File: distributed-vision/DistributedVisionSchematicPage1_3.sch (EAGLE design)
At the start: 114 parts, among them J1 RASPBERRRY_COMPUTE_CM3, J2 RASPBERRRY_COMPUTE_CM3, J3 XS10, J4 10029449-111RLF, J5 10029449-111RLF, Q1 AP2331SA-7, Q2 BSS127, Q3 BSS127, Q4 BJT-NPN_, U1 TPS70625DBVR, U2 LM26420XMH, U3 TPD13S523, U4 ESD224, X1 JST-XH-02-PIN-LONG-PAD

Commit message: Update DistributedVisionSchematicPage1_3.sch
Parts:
- removed U3: TPD13S523, distributed-vision:TPD13S523
- added C14: (no value), rcl:C-USC0603
- added J6: DM3D-SF, distributed-vision:DM3D-SF
- added J7: 10029449-111RLF, distributed-vision:10029449-111RLF
- added Q5: PSMN014-40YS, RoboJackets-Discrete:PSMN014-40YS
- added R56: 47k, RoboJackets-Resistors:ERJ-L06KF50MV
- added RN1, RN2: (no value), RoboJackets-Resistors:RA-82506
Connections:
- new net N$42: J2A.HDMI_CLK_P, J7.10
- new net N$43: J2A.HDMI_CLK_N, J7.12
- new net N$44: J2A.HDMI_SDA, J7.16
- new net N$45: J7.19, Q5.G, R56.PIN2
- net +5V: now also C14.1, J7.18
- net GND: now also C14.2, J7.11, J7.17, J7.2, J7.5, J7.8, Q5.D, R56.PIN1, U4.GND@1, U4.GND@2
- net N$24: now also J7.1; no longer U3.D2+
- net N$25: now also J7.3; no longer U3.D2-
- net N$26: now also J2A.HDMI_D1_P, J7.4; no longer J2A.HDMI_D1_N, U3.D1-
- net N$27: now also J2A.HDMI_D1_N, J7.6; no longer J2A.HDMI_D1_P, U3.D1+
- net N$28: now also J7.7; no longer U3.D0+
- net N$29: now also J7.9; no longer U3.D0-
- net N$30: now also Q5.S
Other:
- note added: "5V FROM USB BOOT"
- note added: "CM1 VBAT = 3v3"
- note added: "CM3 VBAT = 5v"
- note added: "CONNECTOR FOR CAMERA"
- note added: "DAC VCC"
- note added: "DUAL BUCK 1V8 AND 3V3"
- note added: "GPIO BANK0/1 VCC"
- note added: "HDMI POWER"
- note added: "PLACE NEAR COMPUTE MODEL"
- note added: "RASPBERRY PI HEADER"
- note added: "SELECT VBAT for CM1 or CM3"
- note added: "USB BOOT ENABLE"
- moved on the sheet: C10, C102, C103, C12, C13, C15, C17, C18, C19, C21, C22, C23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

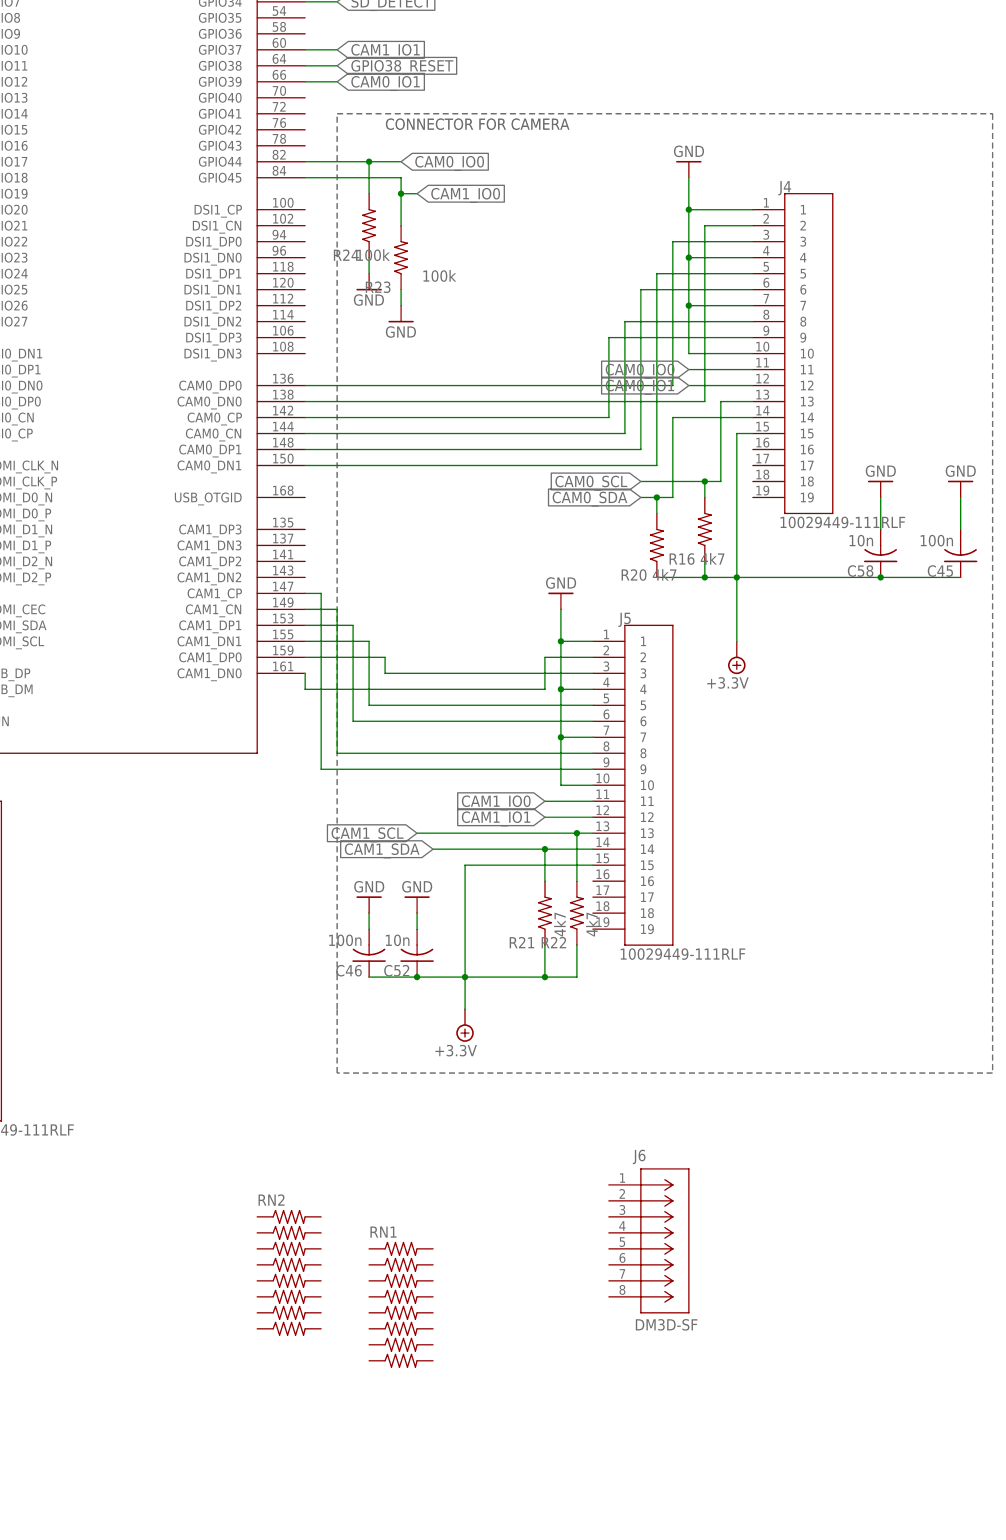
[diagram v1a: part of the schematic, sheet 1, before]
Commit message: Disb Vision Library Edit/Schematic Update
Edited Pins 4,6,10,12,14,16,18,22,24 to SDX_ for MicroSD
Finish Micro_SD part of Schematic on Pg 1
Replaced BJT with JP1 on Pg 3
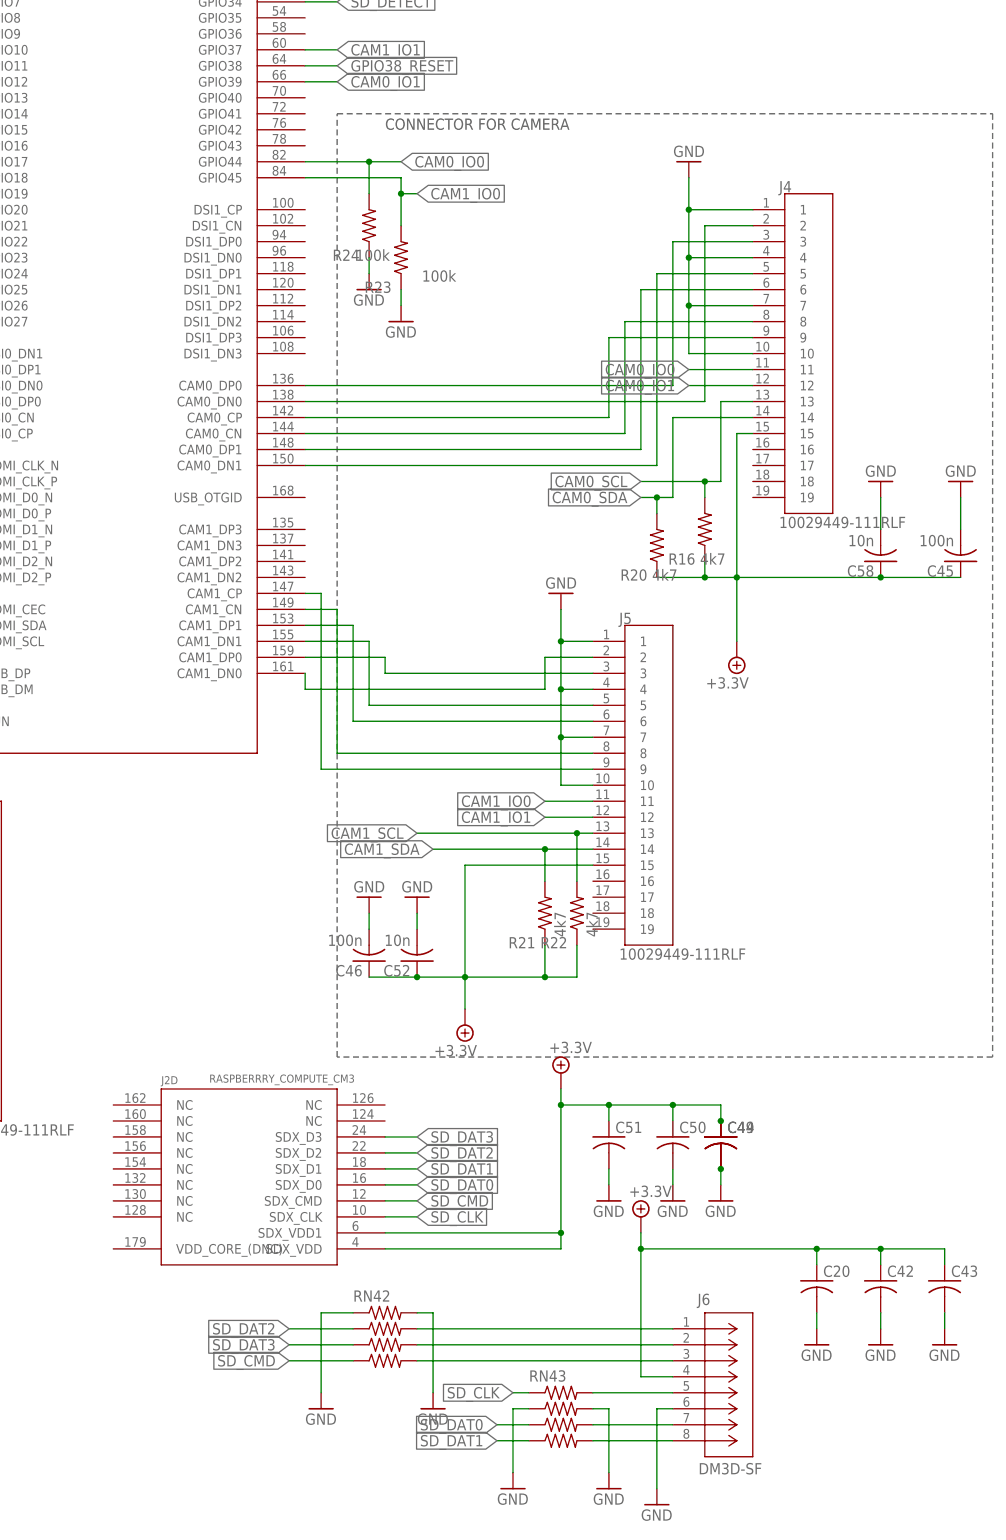
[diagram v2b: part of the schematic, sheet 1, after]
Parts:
- removed L3: (no value), RoboJackets-Inductors:INDUCTOR_0805
- removed Q4: BJT-NPN_, RoboJackets-Discrete:BJT-NPN_
- removed RN1, RN2: (no value), RoboJackets-Resistors:RA-82506
- added C20, C42, C43, C44, C49, C50, C51: (no value), rcl:C-USC0603
- added JP1: (no value), RoboJackets-Connectors:PINHD-1X2
- added L8: 1.3A 120r, RoboJackets-Inductors:INDUCTOR_0805
- added RN42, RN43: (no value), RoboJackets-Resistors:RA-41206
- L1: value 1.3A -> 1uH
- L2: value (none) -> 1uH
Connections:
- new net N$46: J6.1, RN42.4
- new net N$47: J6.2, RN42.6
- new net N$48: J6.3, RN42.8
- new net N$49: J6.5, RN43.2
- new net N$50: J6.7, RN43.6
- new net N$51: J6.8, RN43.8
- new net SD_CLK: J2D.SDX_CLK, RN43.1
- new net SD_CMD: J2D.SDX_CMD, RN42.7
- new net SD_DAT0: J2D.SDX_D0, RN43.5
- new net SD_DAT1: J2D.SDX_D1, RN43.7
- new net SD_DAT2: J2D.SDX_D2, RN42.3
- new net SD_DAT3: J2D.SDX_D3, RN42.5
- net +3.3V: now also C20.1, C42.1, C43.1, C44.1, C49.1, C50.1, C51.1, J2D.SDX_VDD, J2D.SDX_VDD1, J6.4, L8.1, L8.2; no longer L1.1, L3.2
- net +5V: now also JP1.1; no longer Q4.E
- net GND: now also C20.2, C42.2, C43.2, C44.2, C49.2, C50.2, C51.2, J6.6, RN42.1, RN42.2, RN43.3, RN43.4
- net N$33: now also JP1.2; no longer Q4.C
- net N$39: now also L1.1; no longer L3.1
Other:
- moved on the sheet: J6, L1

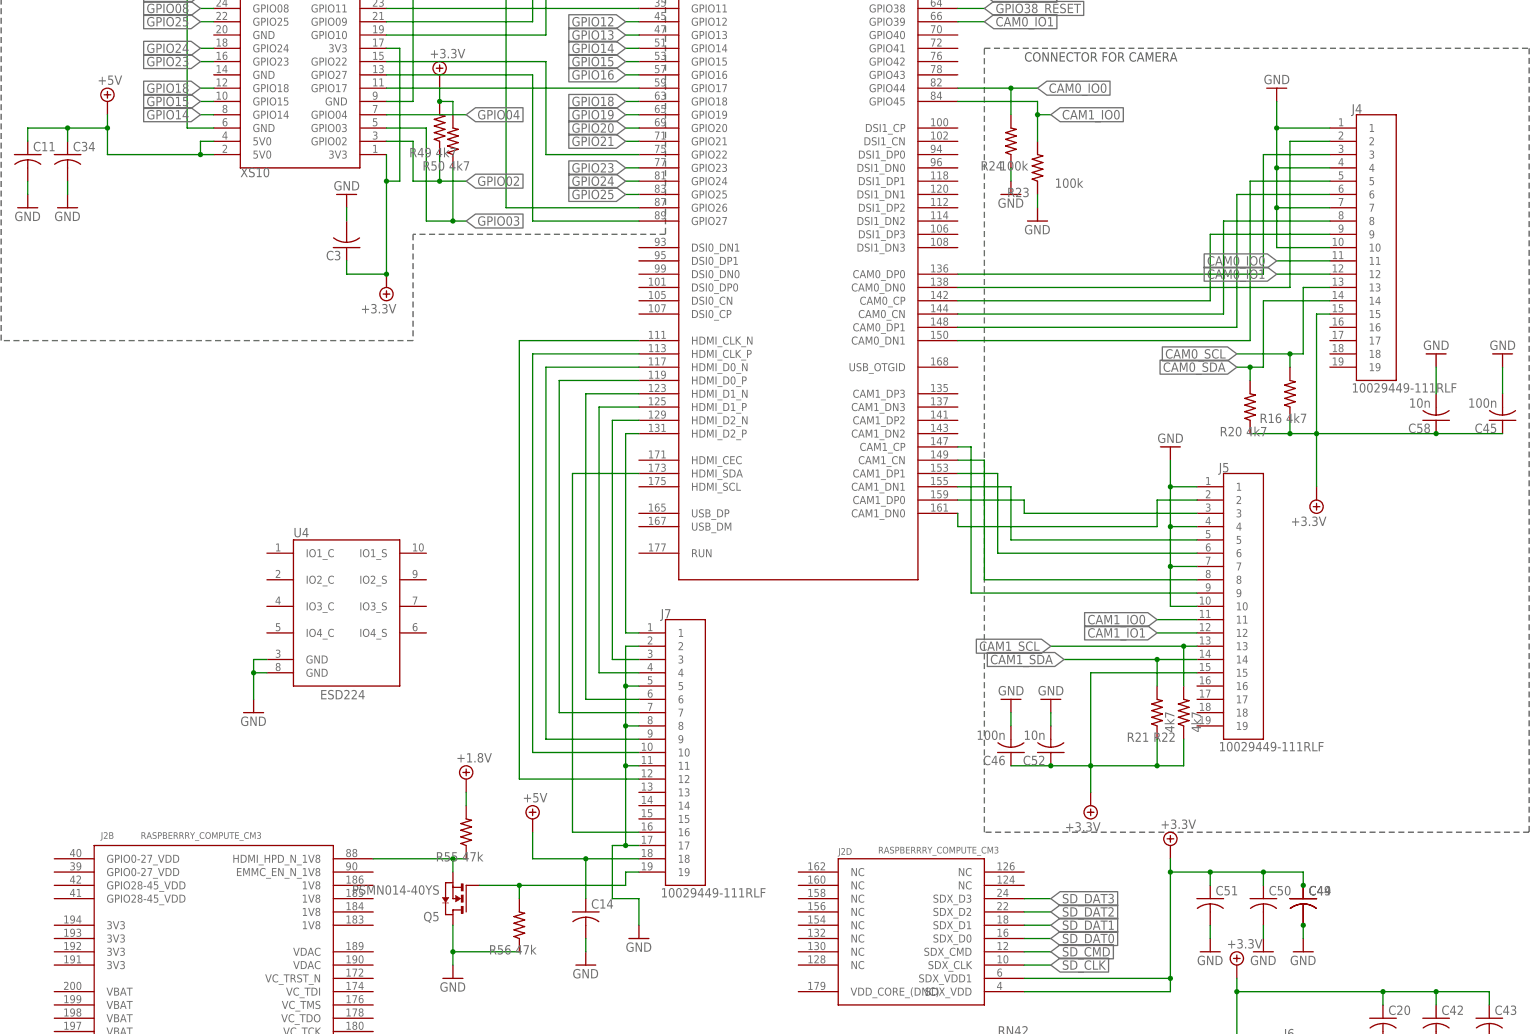
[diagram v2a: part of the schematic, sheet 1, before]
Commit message: Completed Page 1 & 3
Page 3 Unchanged.
Page 1 Edits:
Corrected to 15 pin FPC Connector
Connected ESD224 in HDMI Connector Section
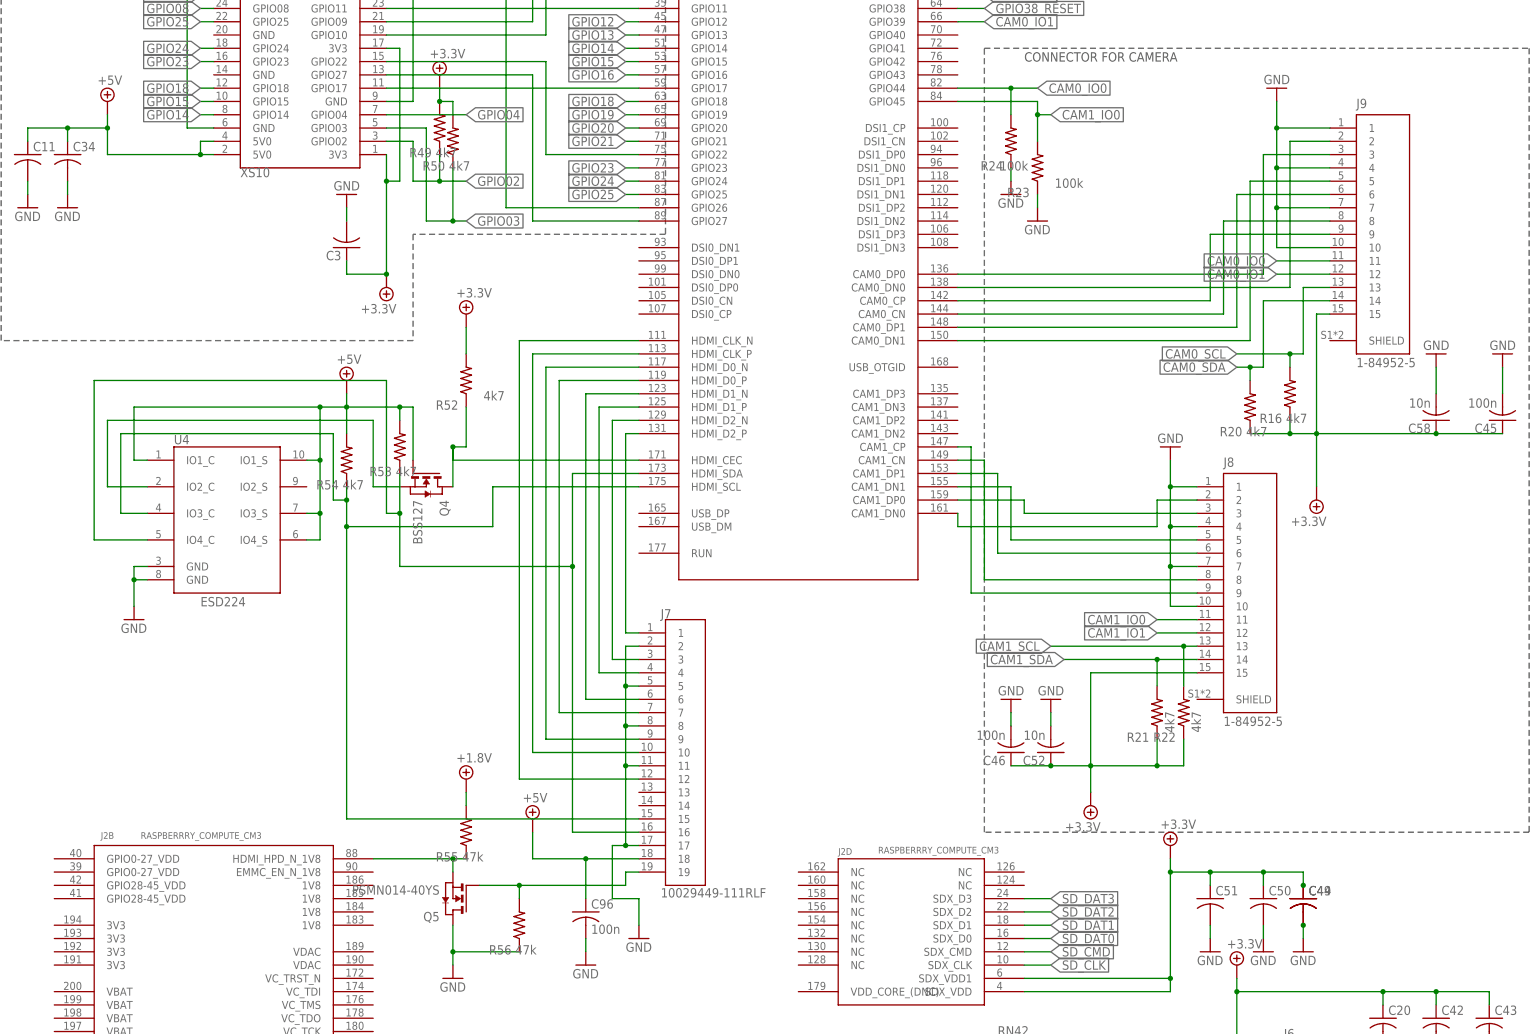
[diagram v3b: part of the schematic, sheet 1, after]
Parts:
- removed J4, J5: 10029449-111RLF, distributed-vision:10029449-111RLF
- added J8, J9: 1-84952-5, 1-84952-5:1-84952-5
- added Q4: BSS127, RoboJackets-Discrete:BSS127
- added R52, R53, R54: 4k7, rcl:R-US_R0603
- C96: value (none) -> 100n
- renumbered C14 to C96
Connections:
- new net N$52: J2A.HDMI_CEC, Q4.D, R52.1
- new net N$53: Q4.S, U4.IO2_C
- new net N$54: J2A.HDMI_SCL, J7.15, R54.1, U4.IO3_C
- net +3.3V: now also J8.15, J9.15, R52.2; no longer J4.15, J5.15
- net +5V: now also Q4.G, R53.2, R54.2, U4.IO1_C, U4.IO1_S, U4.IO3_S, U4.IO4_S
- net CAM0_IO0: now also J9.11; no longer J4.11
- net CAM0_IO1: now also J9.12; no longer J4.12
- net CAM0_SCL: now also J9.13; no longer J4.13
- net CAM0_SDA: now also J9.14; no longer J4.14
- net CAM1_IO0: now also J8.11; no longer J5.11
- net CAM1_IO1: now also J8.12; no longer J5.12
- net CAM1_SCL: now also J8.13; no longer J5.13
- net CAM1_SDA: now also J8.14; no longer J5.14
- net GND: now also J8.1, J8.10, J8.4, J8.7, J9.1, J9.10, J9.4, J9.7; no longer J4.1, J4.10, J4.4, J4.7, J5.1, J5.10, J5.4, J5.7
- net N$12: now also J8.9; no longer J5.9
- net N$13: now also J8.8; no longer J5.8
- net N$14: now also J8.6; no longer J5.6
- net N$15: now also J8.5; no longer J5.5
- net N$16: now also J8.3; no longer J5.3
- net N$17: now also J8.2; no longer J5.2
- net N$18: now also J9.2; no longer J4.2
- net N$19: now also J9.3; no longer J4.3
- net N$20: now also J9.5; no longer J4.5
- net N$21: now also J9.6; no longer J4.6
- net N$22: now also J9.8; no longer J4.8
- net N$23: now also J9.9; no longer J4.9
- net N$44: now also R53.1, U4.IO4_C
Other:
- moved on the sheet: U4

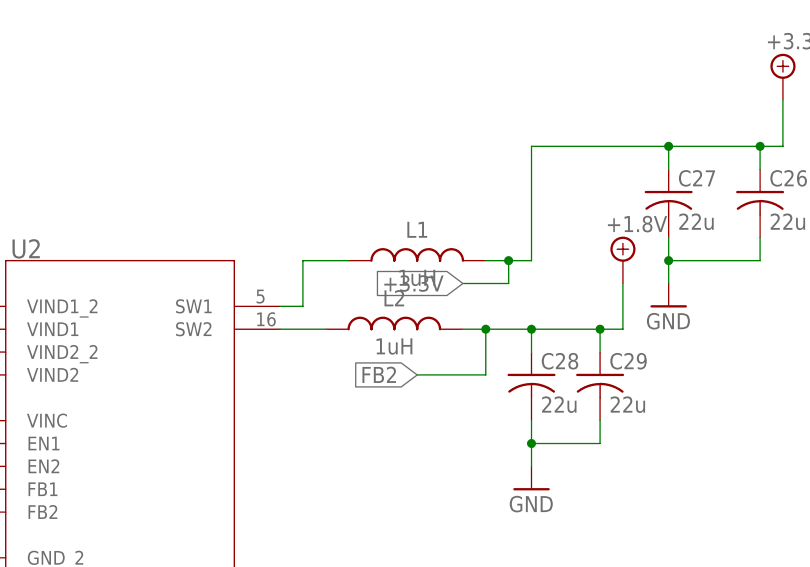
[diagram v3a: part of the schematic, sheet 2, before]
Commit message: Corrected FB1 Label Issue
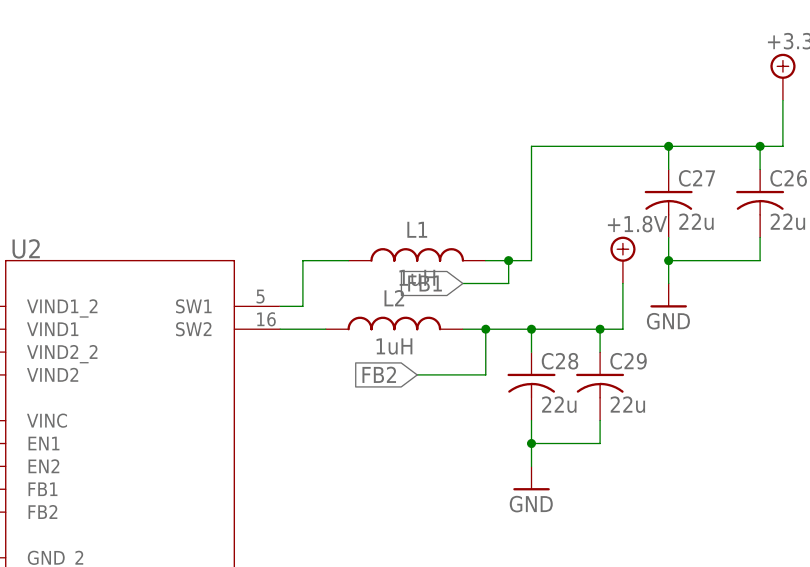
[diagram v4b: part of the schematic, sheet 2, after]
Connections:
- removed net +3.3V: C12.1, C16.1, C20.1, C26.1, C27.1, C3.1, C30.1, C33.1, C4.1, C42.1, C43.1, C44.1, C45.1, C46.1, C49.1, C5.1, C50.1, C51.1, C52.1, C58.1, C6.1, C69.1, C7.1, C70.1, C71.1, C72.1, C76.1, C77.1, C78.1, C79.1, C80.1, C81.1, C82.1, C83.1, C84.1, C85.1, C88.1, C9.1, C91.1, DQ1.A, DQ6.A, J1B.3V3@1, J1B.3V3@2, J1B.3V3@3, J1B.3V3@4, J2D.SDX_VDD, J2D.SDX_VDD1, J3.3V3@1, J3.3V3@2, J6.4, J8.15, J9.15, L1.2, L8.1, L8.2, R16.1, R17.1, R2.1, R20.1, R21.1, R22.1, R45.1, R49.2, R5.1, R50.2, R52.2, U1.EN, U1.IN
- net FB1: now also C12.1, C16.1, C20.1, C26.1, C27.1, C3.1, C30.1, C33.1, C4.1, C42.1, C43.1, C44.1, C45.1, C46.1, C49.1, C5.1, C50.1, C51.1, C52.1, C58.1, C6.1, C69.1, C7.1, C70.1, C71.1, C72.1, C76.1, C77.1, C78.1, C79.1, C80.1, C81.1, C82.1, C83.1, C84.1, C85.1, C88.1, C9.1, C91.1, DQ1.A, DQ6.A, J1B.3V3@1, J1B.3V3@2, J1B.3V3@3, J1B.3V3@4, J2D.SDX_VDD, J2D.SDX_VDD1, J3.3V3@1, J3.3V3@2, J6.4, J8.15, J9.15, L1.2, L8.1, L8.2, R16.1, R17.1, R2.1, R20.1, R21.1, R22.1, R45.1, R49.2, R5.1, R50.2, R52.2, U1.EN, U1.IN
